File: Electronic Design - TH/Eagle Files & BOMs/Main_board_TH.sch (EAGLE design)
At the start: 41 parts, among them M1 ARDUINO-NANO-3.0, Q1 IRF9520, Q2 IRF9520

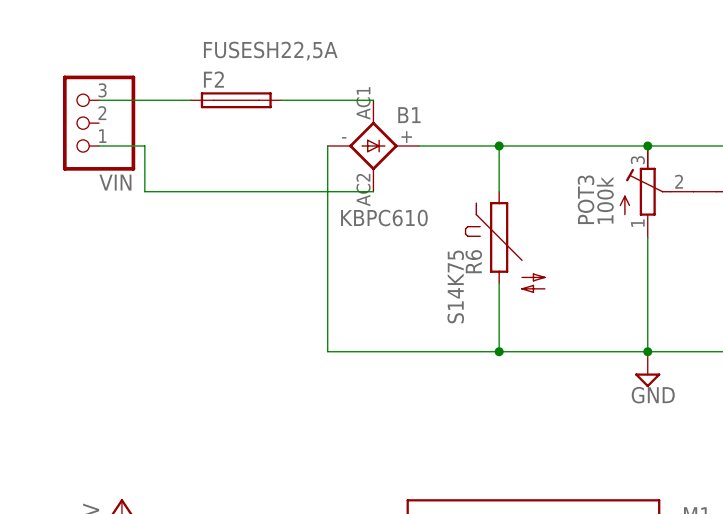
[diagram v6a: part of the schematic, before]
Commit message: Moving fuse to after recification stage
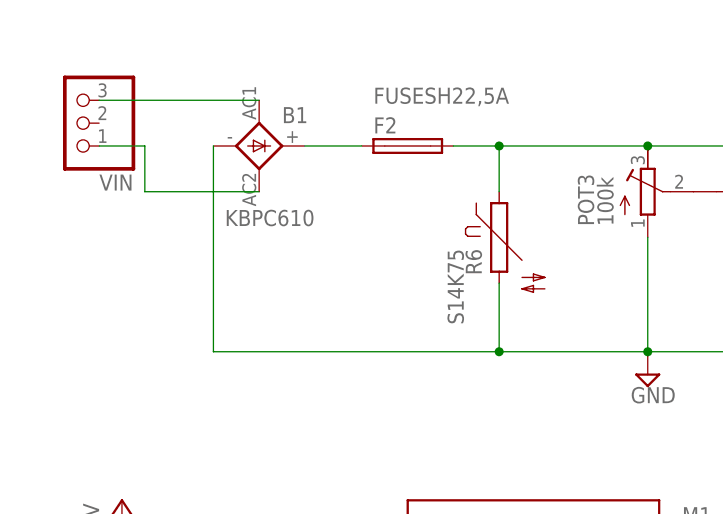
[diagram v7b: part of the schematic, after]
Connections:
- net N$1: now also B1.+; no longer VIN.3
- net N$9: now also VIN.3; no longer F2.2
- net VIN_UNPROTECTED: now also F2.2; no longer B1.+
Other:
- moved on the sheet: B1, F2
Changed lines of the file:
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@@
 </plain>
 <instances>
-<instance part="B1" gate="1" x="-96.52" y="88.9" smashed="yes">
-<attribute name="NAME" x="-93.98" y="91.44" size="1.778" layer="95"/>
-<attribute name="VALUE" x="-100.33" y="80.01" size="1.778" layer="96"/>
+<instance part="B1" gate="1" x="-109.22" y="88.9" smashed="yes">
+<attribute name="NAME" x="-106.68" y="91.44" size="1.778" layer="95"/>
+<attribute name="VALUE" x="-113.03" y="80.01" size="1.778" layer="96"/>
 </instance>
 <instance part="C1" gate="G$1" x="-5.08" y="74.93"/>
@@
 <instance part="Q1" gate="G$1" x="-55.88" y="81.28"/>
 <instance part="Q2" gate="G$1" x="-41.91" y="86.36" rot="R90"/>
-<instance part="F2" gate="G$1" x="-111.76" y="93.98" smashed="yes">
-<attribute name="NAME" x="-115.57" y="95.377" size="1.778" layer="95"/>
-<attribute name="VALUE" x="-115.57" y="98.679" size="1.778" layer="96"/>
+<instance part="F2" gate="G$1" x="-92.71" y="88.9" smashed="yes">
+<attribute name="NAME" x="-96.52" y="90.297" size="1.778" layer="95"/>
+<attribute name="VALUE" x="-96.52" y="93.599" size="1.778" layer="96"/>
 </instance>
 <instance part="U$3" gate="G$1" x="101.6" y="76.2"/>
@@
 <junction x="-66.04" y="66.04"/>
 <pinref part="B1" gate="1" pin="-"/>
-<wire x1="-101.6" y1="88.9" x2="-101.6" y2="66.04" width="0.1524" layer="91"/>
+<wire x1="-114.3" y1="88.9" x2="-114.3" y2="66.04" width="0.1524" layer="91"/>
 <wire x1="-66.04" y1="66.04" x2="-82.55" y2="66.04" width="0.1524" layer="91"/>
-<wire x1="-82.55" y1="66.04" x2="-101.6" y2="66.04" width="0.1524" layer="91"/>
+<wire x1="-82.55" y1="66.04" x2="-114.3" y2="66.04" width="0.1524" layer="91"/>
 <wire x1="-12.7" y1="66.04" x2="-5.08" y2="66.04" width="0.1524" layer="91"/>
 <wire x1="-12.7" y1="71.12" x2="-12.7" y2="66.04" width="0.1524" layer="91"/>
@@
 <pinref part="POT3" gate="G$1" pin="E"/>
 <wire x1="-66.04" y1="88.9" x2="-53.34" y2="88.9" width="0.1524" layer="91"/>
-<pinref part="B1" gate="1" pin="+"/>
 <wire x1="-53.34" y1="88.9" x2="-46.99" y2="88.9" width="0.1524" layer="91"/>
-<wire x1="-91.44" y1="88.9" x2="-82.55" y2="88.9" width="0.1524" layer="91"/>
 <junction x="-66.04" y="88.9"/>
 <pinref part="Q2" gate="G$1" pin="S"/>
@@
 <pinref part="R6" gate="G$1" pin="1"/>
 <wire x1="-82.55" y1="88.9" x2="-82.55" y2="83.82" width="0.1524" layer="91"/>
+<pinref part="F2" gate="G$1" pin="2"/>
+<wire x1="-87.63" y1="88.9" x2="-82.55" y2="88.9" width="0.1524" layer="91"/>
 <junction x="-82.55" y="88.9"/>
 </segment>
@@
 </segment>
 </net>
-<net name="N$1" class="0">
-<segment>
-<pinref part="VIN" gate="A" pin="3"/>
-<pinref part="F2" gate="G$1" pin="1"/>
-<wire x1="-127" y1="93.98" x2="-116.84" y2="93.98" width="0.1524" layer="91"/>
-</segment>
-</net>
 <net name="N$2" class="0">
 <segment>
@@
 <wire x1="-121.92" y1="88.9" x2="-121.92" y2="83.82" width="0.1524" layer="91"/>
 <pinref part="B1" gate="1" pin="AC2"/>
-<wire x1="-121.92" y1="83.82" x2="-96.52" y2="83.82" width="0.1524" layer="91"/>
+<wire x1="-121.92" y1="83.82" x2="-109.22" y2="83.82" width="0.1524" layer="91"/>
+</segment>
+</net>
+<net name="N$1" class="0">
+<segment>
+<pinref part="B1" gate="1" pin="+"/>
+<pinref part="F2" gate="G$1" pin="1"/>
+<wire x1="-104.14" y1="88.9" x2="-97.79" y2="88.9" width="0.1524" layer="91"/>
 </segment>
 </net>
@@
 <segment>
 <pinref part="B1" gate="1" pin="AC1"/>
-<pinref part="F2" gate="G$1" pin="2"/>
-<wire x1="-96.52" y1="93.98" x2="-106.68" y2="93.98" width="0.1524" layer="91"/>
-</segment>
-</net>
+<pinref part="VIN" gate="A" pin="3"/>
+<wire x1="-109.22" y1="93.98" x2="-127" y2="93.98" width="0.1524" layer="91"/>
+</segment>
+</net>

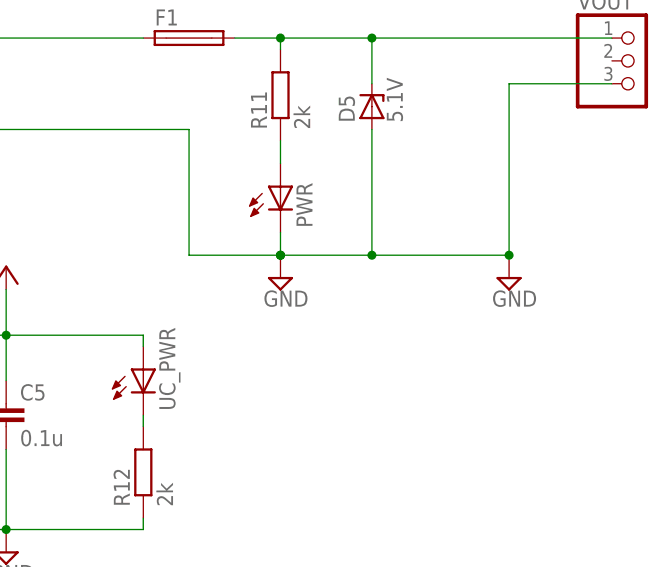
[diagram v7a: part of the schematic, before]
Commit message: removing ground connections from output of LM2596
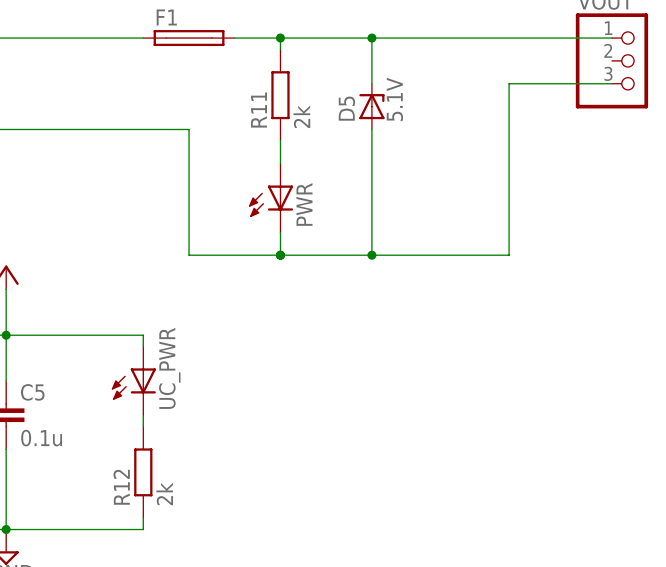
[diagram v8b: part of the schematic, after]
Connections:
- new net N$10: D5.A, PWR.C, U$3.OUT-, VOUT.3
- net GND: no longer D5.A, PWR.C, U$3.OUT-, VOUT.3
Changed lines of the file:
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@@
 <setting verticaltext="up"/>
 </settings>
-<grid distance="0.05" unitdist="inch" unit="inch" style="lines" multiple="1" display="no" altdistance="0.01" altunitdist="inch" altunit="inch"/>
+<grid distance="0.1" unitdist="inch" unit="inch" style="lines" multiple="1" display="no" altdistance="0.01" altunitdist="inch" altunit="inch"/>
 <layers>
 <layer number="1" name="Top" color="4" fill="1" visible="no" active="no"/>
@@
 <part name="D1" library="diode" deviceset="ZPD" device="" value="5.1V"/>
 <part name="R6" library="varistor" deviceset="S14K17" device="" value="S14K75"/>
-<part name="SUPPLY2" library="supply2" deviceset="GND" device=""/>
 <part name="SUPPLY4" library="supply2" deviceset="GND" device=""/>
 <part name="+3V1" library="supply1" deviceset="+5V" device=""/>
@@
 <part name="F2" library="fuse" deviceset="FUSE" device="SH22,5A" value="FUSESH22,5A"/>
 <part name="U$3" library="diy-modules" deviceset="DC-DC-STEP-DOWN-LM2596" device=""/>
-<part name="SUPPLY7" library="supply2" deviceset="GND" device=""/>
 <part name="SUPPLY9" library="supply2" deviceset="GND" device=""/>
 <part name="M1" library="diy-modules" deviceset="ARDUINO-NANO-3.0" device=""/>
@@
 <instance part="D1" gate="G$1" x="-12.7" y="73.66" rot="R90"/>
 <instance part="R6" gate="G$1" x="-82.55" y="78.74" rot="R270"/>
-<instance part="SUPPLY2" gate="GND" x="179.07" y="54.61"/>
 <instance part="SUPPLY4" gate="GND" x="86.36" y="8.89"/>
 <instance part="+3V1" gate="1" x="123.19" y="55.88"/>
@@
 </instance>
 <instance part="U$3" gate="G$1" x="101.6" y="76.2"/>
-<instance part="SUPPLY7" gate="GND" x="153.67" y="54.61"/>
 <instance part="SUPPLY9" gate="GND" x="-5.08" y="63.5"/>
 <instance part="M1" gate="G$1" x="-77.47" y="21.59"/>
@@
 </segment>
 <segment>
-<pinref part="SUPPLY2" gate="GND" pin="GND"/>
-<pinref part="VOUT" gate="A" pin="3"/>
-<wire x1="190.5" y1="76.2" x2="179.07" y2="76.2" width="0.1524" layer="91"/>
-<wire x1="179.07" y1="76.2" x2="179.07" y2="57.15" width="0.1524" layer="91"/>
-<wire x1="163.83" y1="57.15" x2="179.07" y2="57.15" width="0.1524" layer="91"/>
-<junction x="179.07" y="57.15"/>
-<pinref part="D5" gate="G$1" pin="A"/>
-<wire x1="163.83" y1="71.12" x2="163.83" y2="57.15" width="0.1524" layer="91"/>
-<pinref part="PWR" gate="G$1" pin="C"/>
-<wire x1="153.67" y1="59.69" x2="153.67" y2="57.15" width="0.1524" layer="91"/>
-<wire x1="153.67" y1="57.15" x2="163.83" y2="57.15" width="0.1524" layer="91"/>
-<junction x="163.83" y="57.15"/>
-<junction x="153.67" y="57.15"/>
-<pinref part="U$3" gate="G$1" pin="OUT-"/>
-<wire x1="119.38" y1="71.12" x2="143.51" y2="71.12" width="0.1524" layer="91"/>
-<wire x1="143.51" y1="71.12" x2="143.51" y2="57.15" width="0.1524" layer="91"/>
-<wire x1="143.51" y1="57.15" x2="153.67" y2="57.15" width="0.1524" layer="91"/>
-<junction x="153.67" y="57.15"/>
-<pinref part="SUPPLY7" gate="GND" pin="GND"/>
-</segment>
-<segment>
 <pinref part="R8" gate="G$1" pin="1"/>
 <pinref part="SUPPLY4" gate="GND" pin="GND"/>
@@
 </segment>
 </net>
+<net name="N$10" class="0">
+<segment>
+<pinref part="VOUT" gate="A" pin="3"/>
+<wire x1="190.5" y1="76.2" x2="179.07" y2="76.2" width="0.1524" layer="91"/>
+<wire x1="179.07" y1="76.2" x2="179.07" y2="57.15" width="0.1524" layer="91"/>
+<wire x1="163.83" y1="57.15" x2="179.07" y2="57.15" width="0.1524" layer="91"/>
+<pinref part="D5" gate="G$1" pin="A"/>
+<wire x1="163.83" y1="71.12" x2="163.83" y2="57.15" width="0.1524" layer="91"/>
+<pinref part="PWR" gate="G$1" pin="C"/>
+<wire x1="153.67" y1="59.69" x2="153.67" y2="57.15" width="0.1524" layer="91"/>
+<wire x1="153.67" y1="57.15" x2="163.83" y2="57.15" width="0.1524" layer="91"/>
+<junction x="163.83" y="57.15"/>
+<junction x="153.67" y="57.15"/>
+<pinref part="U$3" gate="G$1" pin="OUT-"/>
+<wire x1="119.38" y1="71.12" x2="143.51" y2="71.12" width="0.1524" layer="91"/>
+<wire x1="143.51" y1="71.12" x2="143.51" y2="57.15" width="0.1524" layer="91"/>
+<wire x1="143.51" y1="57.15" x2="153.67" y2="57.15" width="0.1524" layer="91"/>
+<junction x="153.67" y="57.15"/>
+</segment>
+</net>
